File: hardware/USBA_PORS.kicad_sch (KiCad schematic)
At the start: 29 parts, among them J3 0483930003, J4 0483930003, J5 0483930003, J6 0483930003, U13 USB5926C

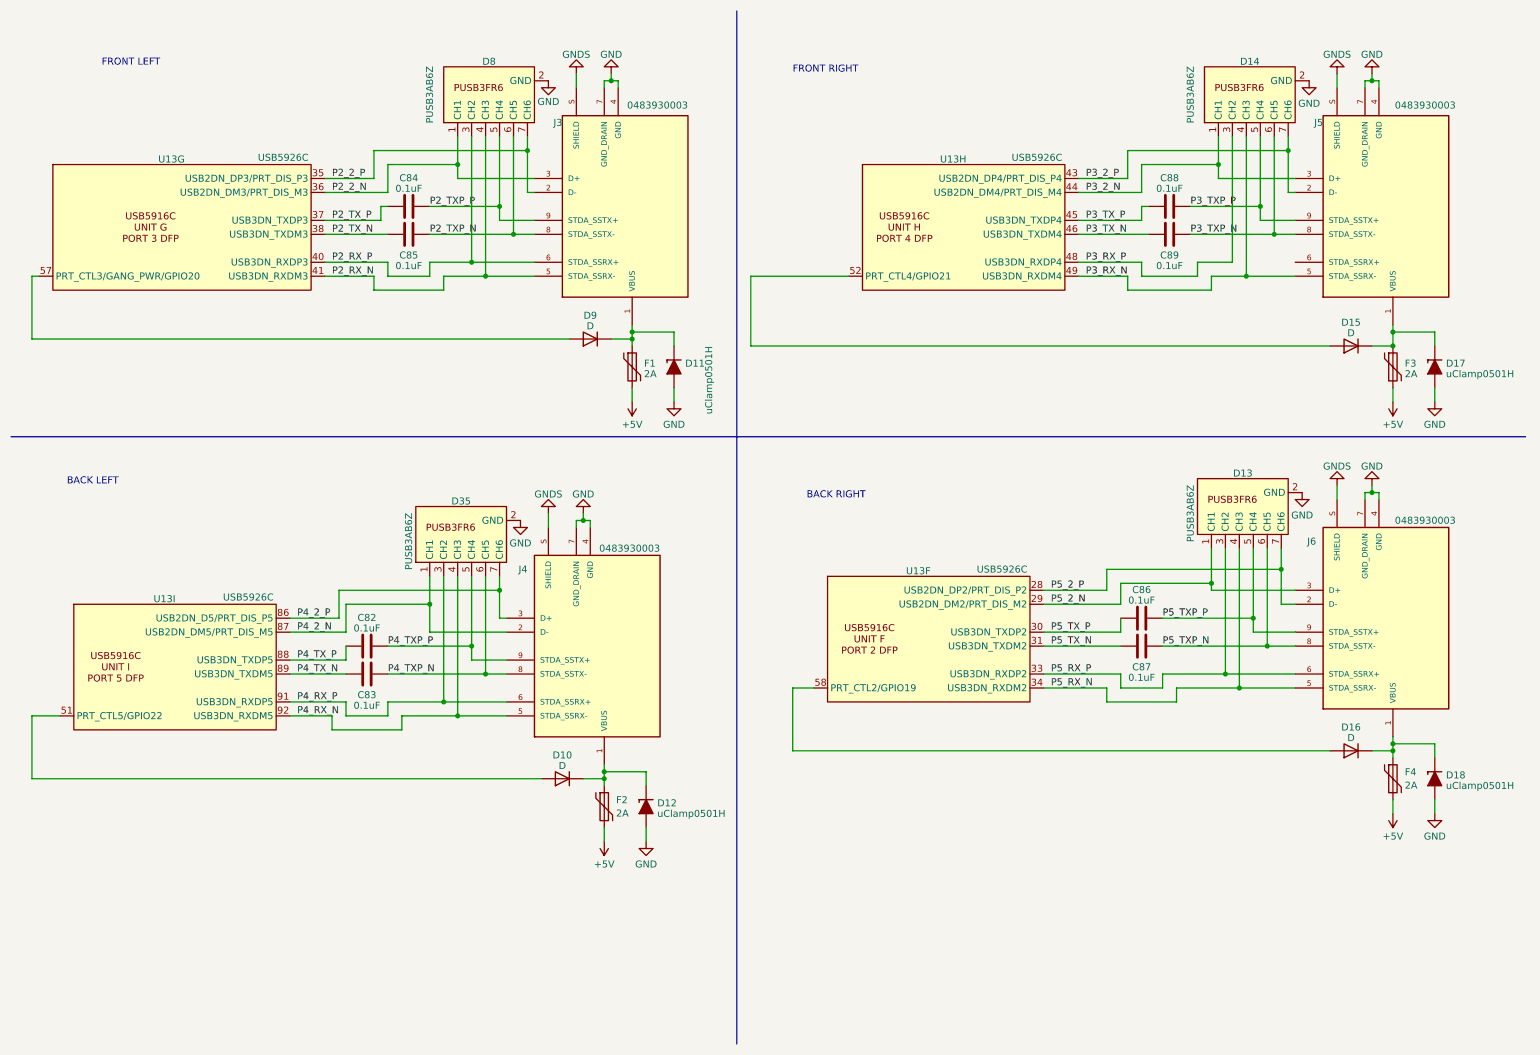
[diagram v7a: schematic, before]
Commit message: updated block digram minor pcb changes
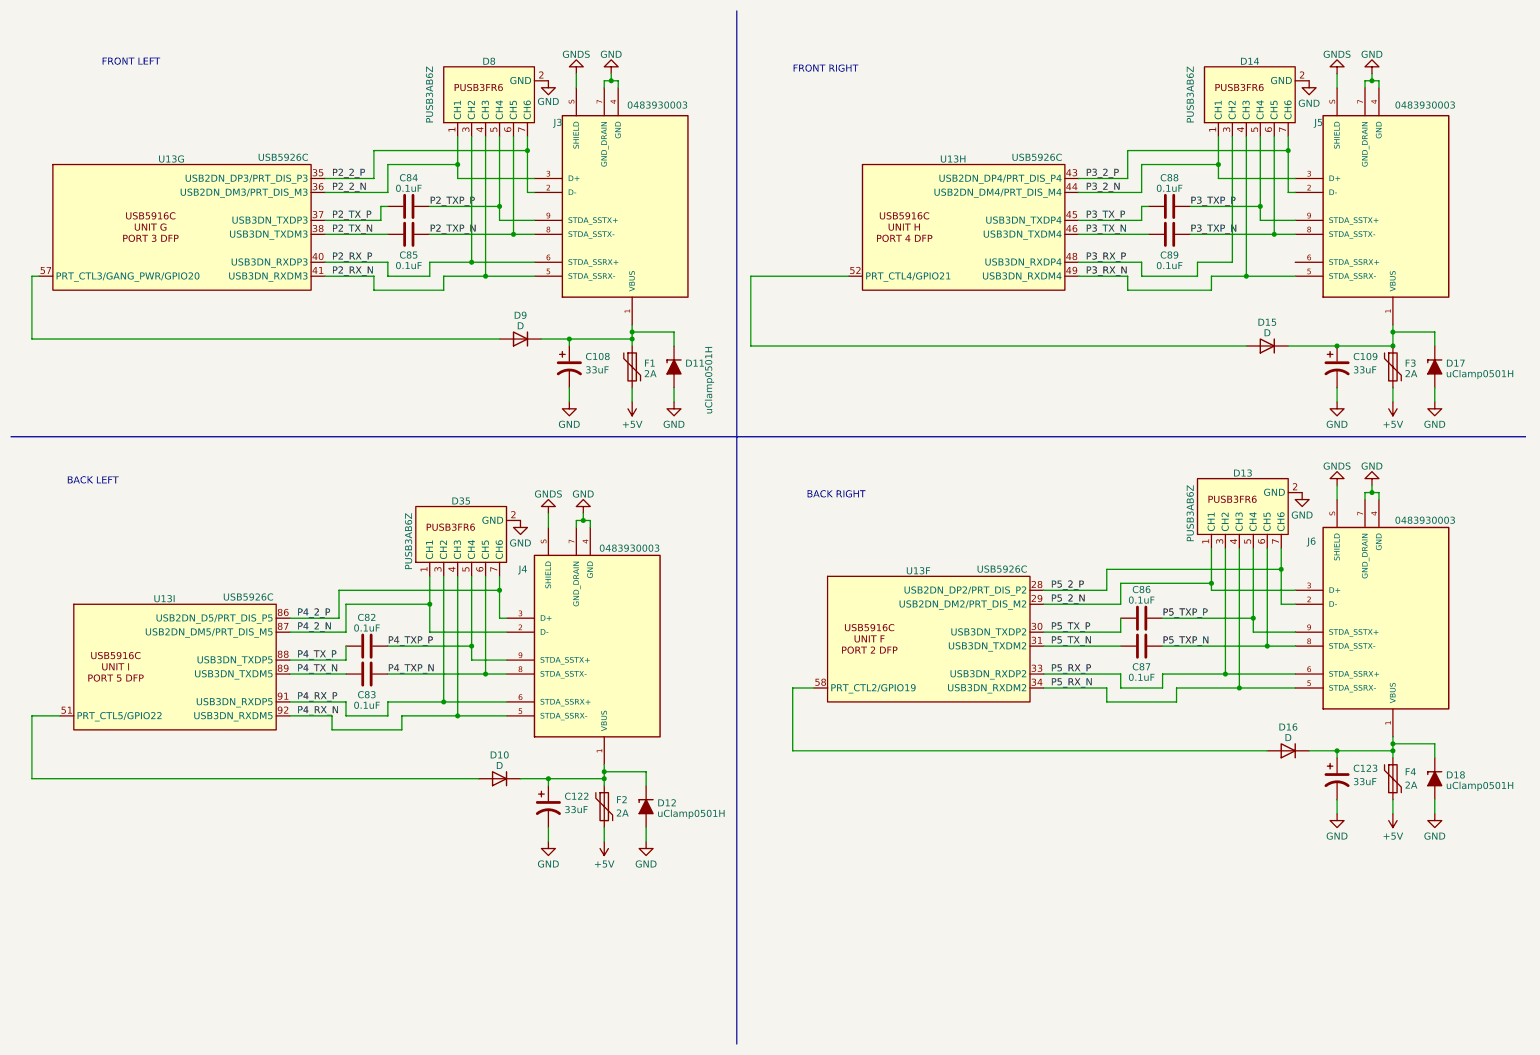
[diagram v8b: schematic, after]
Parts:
- added C108, C109, C122, C123: 33uF, Capacitor_SMD:C_Elec_6.3x5.8, symbol Device:C_Polarized_US
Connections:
- net GND: now also C108.2, C109.2, C122.2, C123.2
- net at D10.1 (K), D12.1 (K), F2.1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: now also C122.1
- net at D16.1 (K), D18.1 (K), F4.1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: now also C123.1
- net at D11.1 (K), D9.1 (K), F1.1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: now also C108.1
- net at D15.1 (K), D17.1 (K), F3.1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: now also C109.1
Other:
- moved on the sheet: D10, D15, D16, D9
